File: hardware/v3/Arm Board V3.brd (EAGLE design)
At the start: 165.1 x 76.2 mm, 44 parts, among them CN1 1X4-BIG, IC1 L6208D, IC2 L6208D, IC3 L6208D, Q3 Q_LTC490, U1 MAX3468CSA

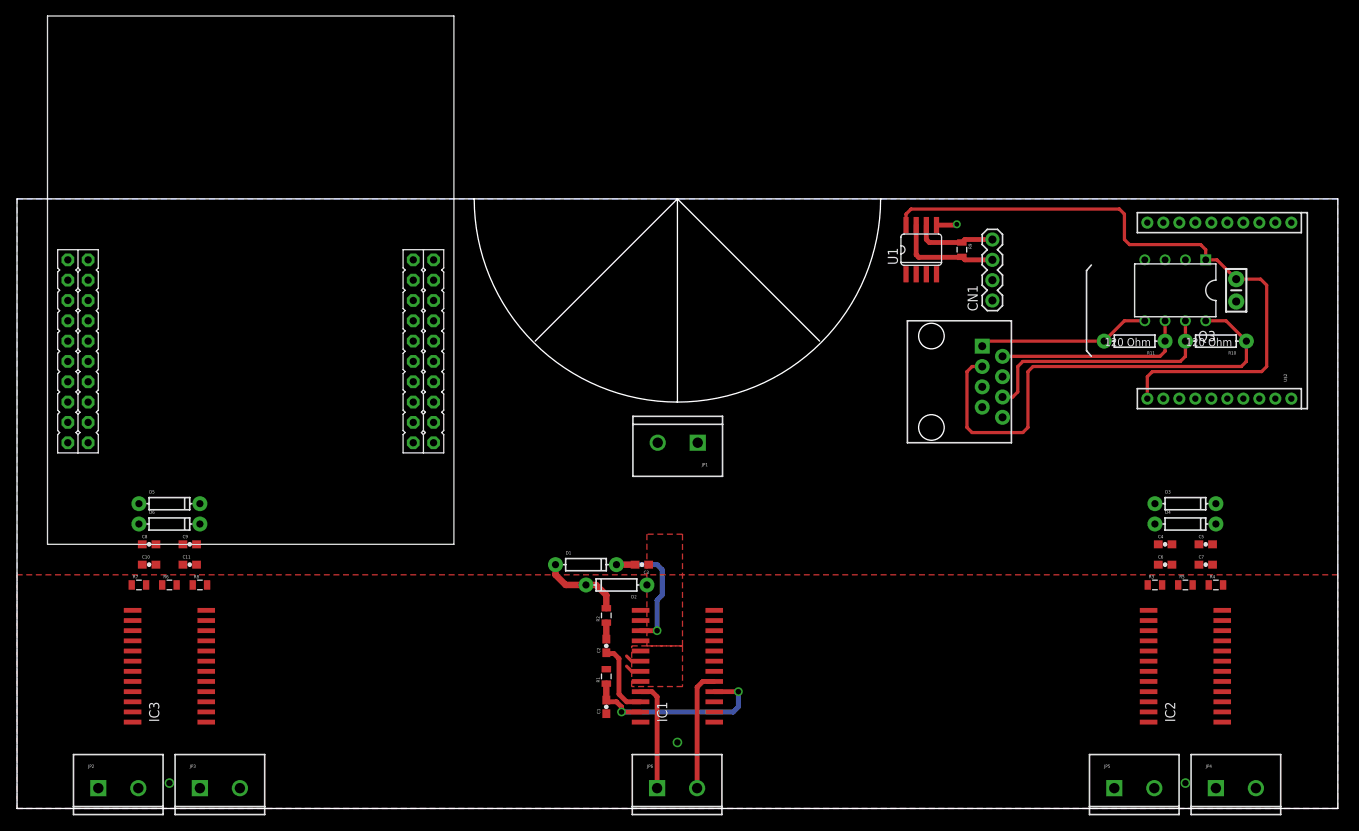
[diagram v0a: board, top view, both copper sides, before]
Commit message: Started assigning serial pins and routing
Also added picture of TI Launchpad pinout (It will be fun when it comes
time to add encoders)
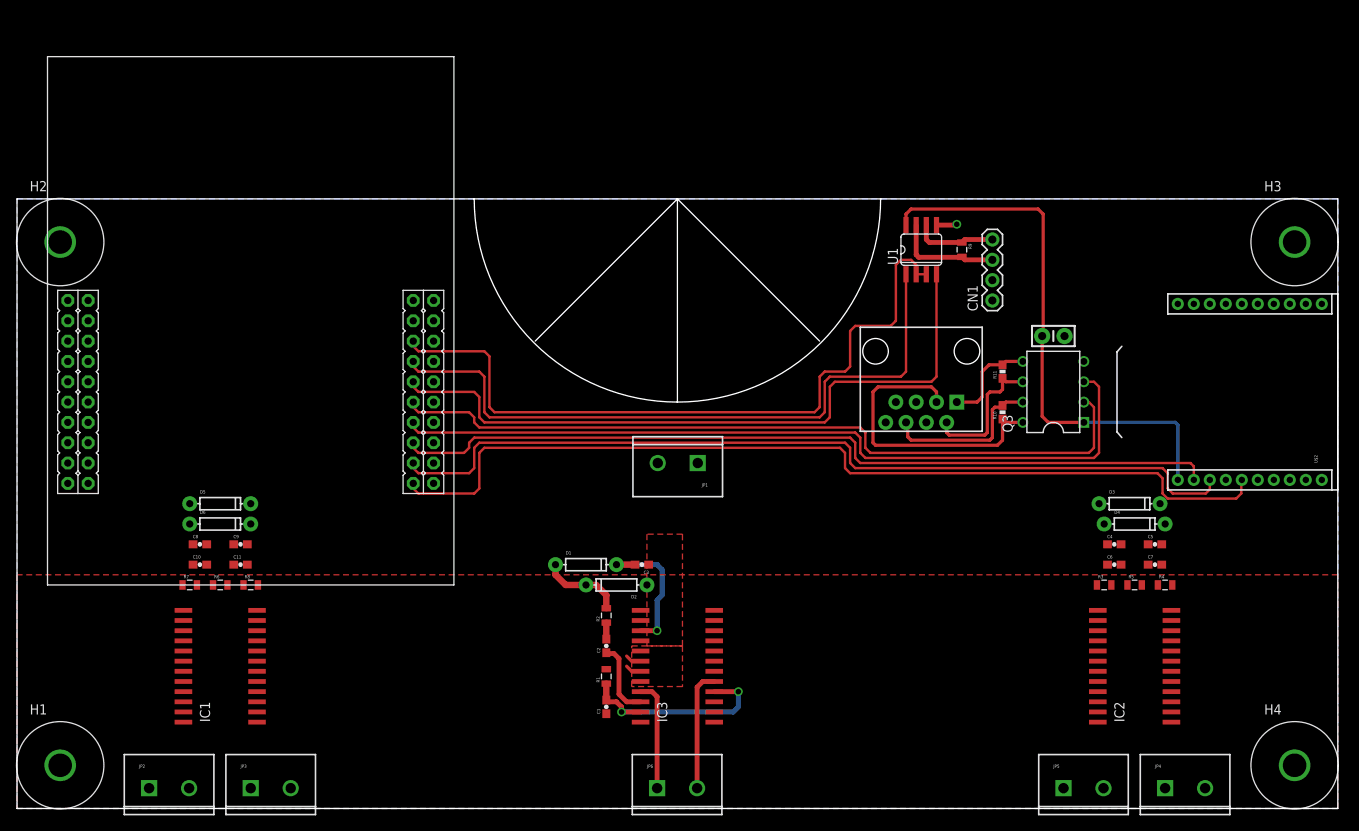
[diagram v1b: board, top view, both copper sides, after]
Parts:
- added H1, H2, H3, H4: (no value), Lib_TH:H_MNTHOLE_#4
- R10, R11: device SparkFun-Passives:AXIAL-0.3 -> SparkFun-Passives:0603-RES
- moved IC3 63.5 mm to (82.5, 17.8)
- moved IC1 57.1 mm to (25.4, 17.8)
- moved R10 28.1 mm to (123.2, 49.5), turned to 90 degrees
- moved C12 23.6 mm to (129.5, 59.1), turned to 0 degrees
- moved Q3 19.8 mm to (129.5, 52.1), turned to 90 degrees
- moved R11 16.9 mm to (123.2, 54.6), turned to 90 degrees
- moved U$2 10.9 mm to (165.1, 52.1)
- moved D3 6.99 mm to (139.1, 38.1)
- moved D4 6.35 mm to (139.7, 35.6)
- moved IC2 6.35 mm to (139.7, 17.8)
- moved JP4 6.35 mm to (143.5, 2.54)
- moved R3 6.35 mm to (135.9, 27.9)
- moved R4 6.35 mm to (143.5, 27.9)
- moved R5 6.35 mm to (139.7, 27.9)
- moved C11 6.35 mm to (27.9, 30.5)
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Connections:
- net +12V renamed +18V
- net PIN25 renamed IN1_A_2
- net PIN26 renamed IN2_A_2
- net PIN27 renamed IN1_B_2
- net PIN28 renamed IN2_B_2
- net PIN29 renamed IN1_A_1
- net PIN30 renamed IN2_A_1
- net PIN44 renamed IN1_A_3
- net PIN45 renamed IN2_A_3
- net PWM5 renamed EN_A_2
- net PWM6 renamed EN_B_2
- net PWM7 renamed EN_A_3
- net PWM8 renamed EN_A_1
- net PWM9 renamed EN_B_1
- net RST renamed RESET
- removed net +5V: C12.1, Q3.1, U$2.1, U1.8
- removed net DM: Q3.3
- removed net GND2: U$1.GND2
- removed net PIN23: U1.2, U1.3
- removed net PIN46: IC3.11
- removed net PIN47: IC3.12
- removed net RM: Q3.2
- new net EN485: U$1.PB3, U1.2, U1.3
- new net IN1_B_1: IC1.11
- new net IN2_B_1: IC1.12
- new net RXD3: U$1.PD6, U$2.2
- new net TXD3: U$1.PD7, U$2.3
- new net XRESET: U$1.PF4, U$2.5
- net +3V3: now also C12.1, Q3.1, U$2.1, U1.8
- net A1_1: now also IC1.5; no longer IC3.5
- net A1_3: now also IC3.5; no longer IC1.5
- net A2_1: now also IC1.21; no longer IC3.21
- net A2_3: now also IC3.21; no longer IC1.21
- net B1_1: now also IC1.8; no longer IC3.8
- net B2_1: now also IC1.16; no longer IC3.16
- net GND: now also H1.1, H2.1, H3.1, H4.1, U$1.GND1, U$1.GND2
- net N$1: now also R11.1; no longer R11.P$1
- net N$13: now also IC1.22; no longer IC3.22
- net N$19: now also IC3.22; no longer IC1.22
- net N$2: now also R10.2; no longer R10.P$2
- net N$3: now also R10.1; no longer R10.P$1
- net N$5: now also R11.2; no longer R11.P$2
- net OCD_A_1: now also IC1.23, IC1.4; no longer IC3.23, IC3.4
- net OCD_A_3: now also IC3.23, IC3.4; no longer IC1.23, IC1.4
- net OCD_B_1: now also IC1.14, IC1.9; no longer IC3.14, IC3.9
- net RXD1: now also Q3.2, U$1.PC6; no longer U1.1
- net RXD2: now also U$1.PC4, U1.1; no longer U$2.2
- net TXD1: now also Q3.3, U$1.PC7; no longer U1.4
- net TXD2: now also U$1.PC5, U1.4; no longer U$2.3
- net VBOOT_1: now also IC1.15; no longer IC3.15
- net VBOOT_3: now also IC3.15; no longer IC1.15
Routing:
- net XRESET: track 0.00 -> 116.2 mm
- net TXD3: track 0.00 -> 109.8 mm
- net RXD3: track 0.00 -> 103.9 mm
- net TXD1: track 0.00 -> 99.7 mm
- net RXD1: track 0.00 -> 96.5 mm
- net EN485: track 0.00 -> 90.2 mm
- net TXD2: track 0.00 -> 86.8 mm
- net RXD2: track 0.00 -> 84.3 mm
- net +5V: track 81.6 -> 0.00 mm
- net +3V3: track 0.00 -> 68.6 mm
- net N$3: track 60.8 -> 38.0 mm
- net N$2: track 31.3 -> 20.2 mm
- net N$5: track 21.6 -> 12.2 mm
- net N$1: track 24.4 -> 17.9 mm
- net GND: vias 4 -> 1

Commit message: Added enable pins to schematic and routed
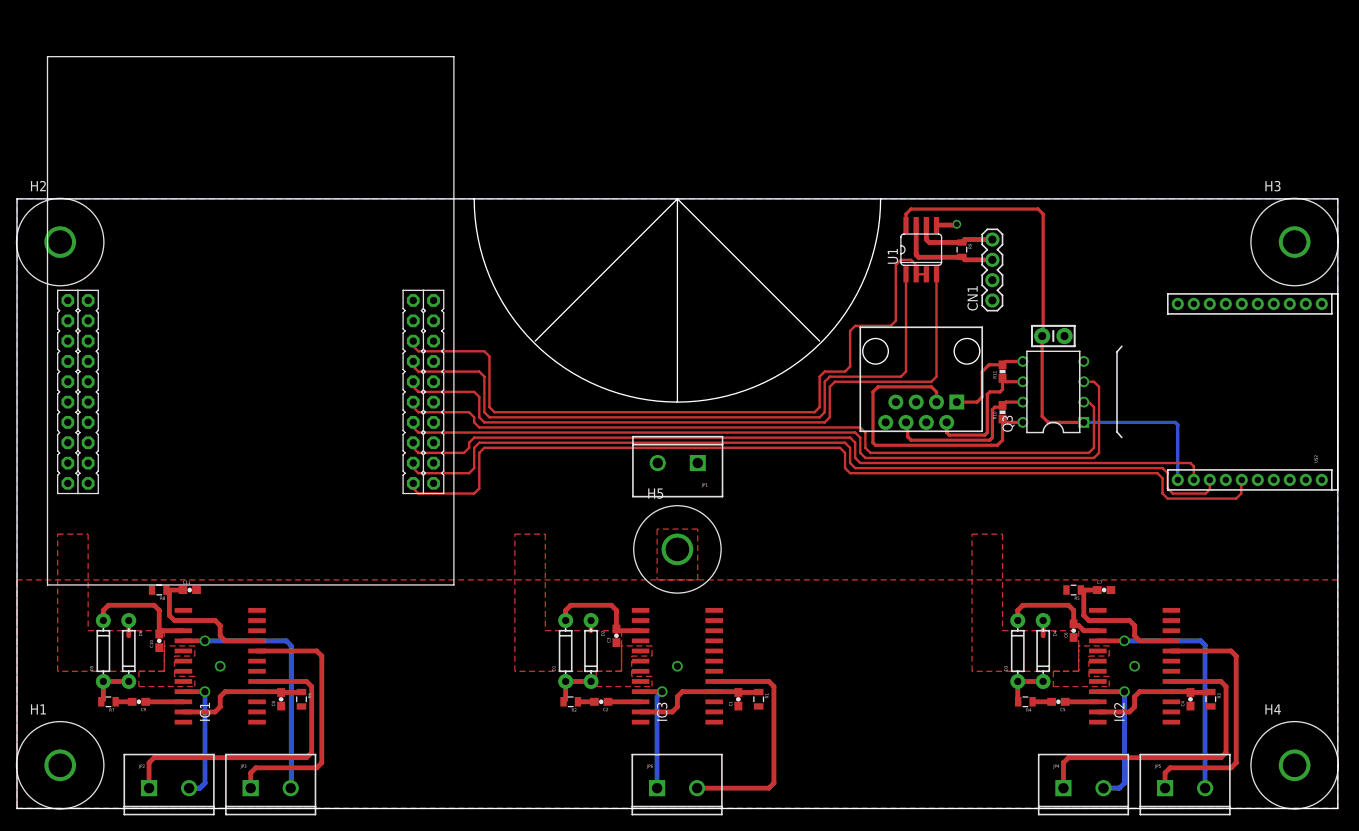
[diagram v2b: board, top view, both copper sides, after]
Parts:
- added H5: (no value), Lib_TH:H_MNTHOLE_#4
- moved D5 23.5 mm to (10.8, 19.7), turned to 90 degrees
- moved C9 23.4 mm to (15.2, 13.3), turned to 180 degrees
- moved D3 23.1 mm to (125.1, 19.7), turned to 90 degrees
- moved C5 23.1 mm to (130.2, 13.3), turned to 180 degrees
- moved R4 22.8 mm to (126.0, 13.3), turned to 180 degrees
- moved C8 21.9 mm to (33.0, 13.7), turned to 90 degrees
- moved C4 21.6 mm to (146.7, 13.7), turned to 90 degrees
- moved D6 19.6 mm to (14.0, 19.7), turned to 270 degrees
- moved D4 19.6 mm to (128.3, 19.7), turned to 270 degrees
- moved R3 19.5 mm to (149.2, 13.7), turned to 270 degrees
- moved R1 19.3 mm to (92.7, 13.7), turned to 270 degrees
- moved R7 17.8 mm to (11.4, 13.3), turned to 180 degrees
- moved R6 17.5 mm to (35.6, 13.7), turned to 270 degrees
- moved C1 16.5 mm to (90.2, 13.7)
- moved JP4 12.7 mm to (130.8, 2.54)
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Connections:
- net EN_A_1: now also U$1.PA7
- net EN_A_2: now also U$1.PE3
- net EN_A_3: now also U$1.PA5
- net EN_B_1: now also U$1.PA6
- net EN_B_2: now also U$1.PE2
- net GND: now also H5.1
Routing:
- net A1_1: track 0.00 -> 39.4 mm
- net A1_2: track 0.00 -> 39.4 mm
- net B1_1: track 0.00 -> 33.0 mm
- net B1_2: track 0.00 -> 33.0 mm
- net B2_1: track 0.00 -> 31.6 mm, vias 0 -> 1
- net B2_2: track 0.00 -> 31.5 mm, vias 0 -> 1
- net OCD_B_2: track 0.00 -> 18.4 mm
- net OCD_B_1: track 0.00 -> 18.4 mm
- net A2_2: track 0.00 -> 17.6 mm, vias 0 -> 1
- net OCD_A_1: track 0.00 -> 16.6 mm
- net A2_1: track 0.00 -> 16.4 mm, vias 0 -> 1
- net OCD_A_2: track 0.00 -> 16.0 mm
- net VBOOT_1: track 0.00 -> 14.9 mm
- net A1_3: track 15.1 -> 29.7 mm
- net VBOOT_2: track 0.00 -> 13.8 mm
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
